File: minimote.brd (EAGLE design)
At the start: 85.6 x 54.2 mm, 44 parts, among them IC1 ATTINY841, J1 AVR_SPI_PROG_3X2PTH, J2 EDGEUSB, P1 TOUCHPAD, P2 TOUCHPAD, P3 TOUCHPAD, P4 TOUCHPAD, P5 TOUCHPAD, P6 TOUCHPAD, P7 TOUCHPAD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

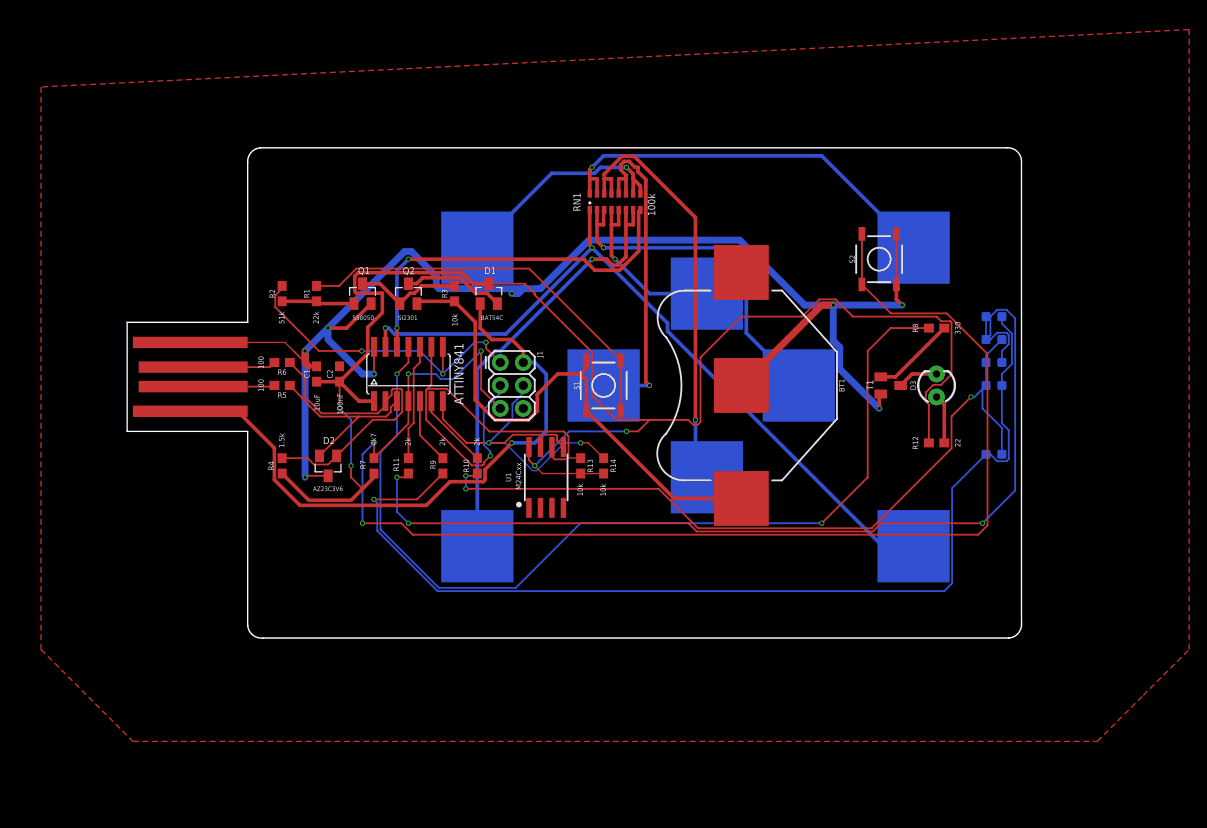
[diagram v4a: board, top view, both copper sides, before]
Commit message: Some board revisions and first firmware checkin
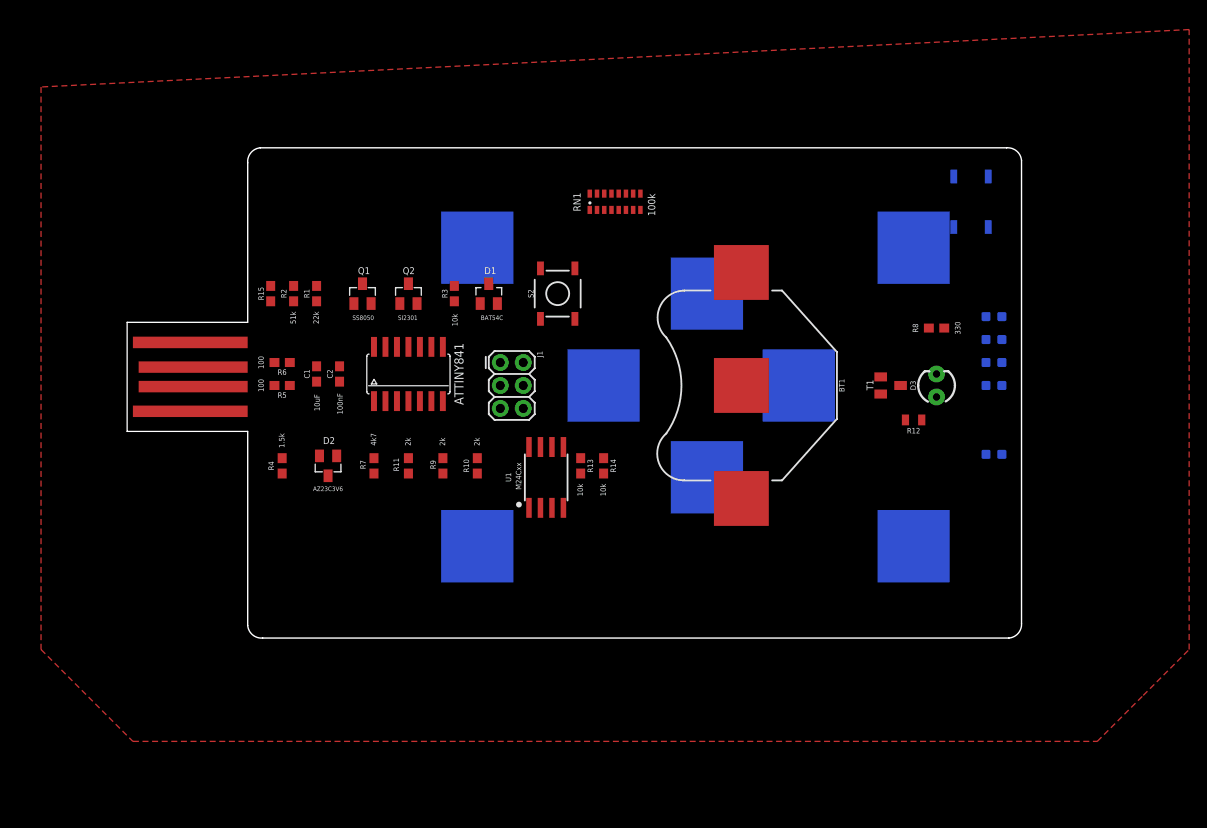
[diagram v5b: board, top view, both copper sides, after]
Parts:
- added R15: 100k, SparkFun-Resistors:0603
- R12: device SparkFun-Resistors:0603 -> SparkFun-Resistors:0805
- moved S1 45.4 mm to (80.0, 48.3), flipped to the bottom
- moved S2 35.8 mm to (34.3, 38.1)
- moved R12 3.59 mm to (73.7, 24.1), turned to 180 degrees
- moved R2 1.27 mm to (5.08, 38.1)
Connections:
- removed net N$5: D1.2, Q2.3
- new net LEDVCC: D1.2, Q2.3, R12.2
- net D_M: no longer D2.2
- net D_P: no longer D2.1, R4.1
- net GND: now also R15.1
- net MISO: now also R15.2
- net N$1: now also R12.1; no longer R12.2
- net N$8: now also D2.1, J2.DP, R6.2; no longer J2.DM, R5.2
- net N$9: now also D2.2, J2.DM, R4.1, R5.2; no longer J2.DP, R6.2
- net VCC: no longer R12.1
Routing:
- net VCC: track 176.8 -> 0.00 mm, vias 4 -> 0
- net GND: track 167.5 -> 0.00 mm, vias 8 -> 0
- net RST: track 150.4 -> 0.00 mm, vias 4 -> 0
- net N$125: track 114.9 -> 0.00 mm, vias 1 -> 0
- net N$123: track 110.5 -> 0.00 mm, vias 3 -> 0
- net LED4: track 104.9 -> 0.00 mm, vias 2 -> 0
- net N$124: track 85.3 -> 0.00 mm, vias 3 -> 0
- net PAD0: track 83.2 -> 0.00 mm, vias 2 -> 0
- net V_USB: track 69.0 -> 0.00 mm, vias 1 -> 0
- net VBAT: track 59.2 -> 0.00 mm
- net SCK: track 51.5 -> 0.00 mm, vias 1 -> 0
- net PAD6: track 49.4 -> 0.00 mm, vias 1 -> 0
- net PAD3: track 47.6 -> 0.00 mm, vias 1 -> 0
- net PAD1: track 45.8 -> 0.00 mm, vias 1 -> 0
- net N$7: track 44.2 -> 0.00 mm
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
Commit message: major pcb revisions
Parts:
- removed BT1: (no value), SparkFun-Batteries:BATTCON_20MM
- removed P1, P2, P3, P4, P5, P6, P7, P8: TOUCHPAD, minimote:TPAD
- added R16: 22M, SparkFun-Resistors:0603
- added U$1: BAT_AND_USB, minimote:PUNCHOUT_USB
- added U$2, U$3, U$4, U$5, U$6, U$7, U$8, U$9: BUTTON_RESISTIVE, minimote:BUTTON-CONDUCTIVE
- RN1: value 100k -> 10k
- moved R12 58.8 mm to (15.2, 30.5)
- moved R8 55.4 mm to (24.1, 53.3)
- moved T1 46.2 mm to (31.8, 52.1)
- moved S1 43.2 mm to (81.3, 5.08)
- moved R4 33.0 mm to (12.7, 50.8), turned to 90 degrees
- moved D2 32.5 mm to (8.38, 51.6), turned to 90 degrees
- moved U1 32.4 mm to (19.1, 47.0), turned to 270 degrees
- moved RN1 32.3 mm to (17.8, 25.4)
- moved R10 24.3 mm to (8.89, 36.8)
- moved J2 20.9 mm to (5.08, 43.2)
- moved R2 20.4 mm to (25.4, 36.8)
- moved R1 19.4 mm to (26.7, 41.9)
- moved R13 19.1 mm to (25.4, 3.81)
- moved R14 19.0 mm to (27.9, 3.81)
- moved R15 18.8 mm to (19.1, 29.2)
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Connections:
- removed net PAD0: IC1.13, P1.P$1, RN1.1
- removed net TOUCH2: IC1.12, RN1.8
- new net PA1: IC1.12
- new net PAD_HIGH: IC1.13, R16.1, U$2.2, U$3.2, U$4.2, U$5.2, U$6.2, U$7.2, U$8.2, U$9.2
- net GND: now also RN1.8, U$1.B-, U$2.1; no longer BT1.2
- net PAD1: now also U$3.1; no longer P2.P$1
- net PAD2: now also U$4.1; no longer P3.P$1
- net PAD3: now also U$5.1; no longer P4.P$1
- net PAD4: now also U$6.1; no longer P5.P$1
- net PAD5: now also U$7.1; no longer P6.P$1
- net PAD6: now also U$8.1; no longer P7.P$1
- net PAD7: now also U$9.1; no longer P8.P$1
- net VBAT: now also U$1.B+; no longer BT1.1
- net VCC: now also R16.2, RN1.1
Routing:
- added copper zone on layer 16, net GND
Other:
- outline, holes or cut-outs redrawn

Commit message: added library
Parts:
- moved D3 15.2 mm to (82.5, 25.4)
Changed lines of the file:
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@@
 <attribute name="VALUE" x="28.575" y="53.975" size="1.27" layer="27" rot="R270"/>
 </element>
-<element name="D3" library="minimote" package="LED_3MM" value="" x="82.55" y="40.64" rot="R90">
-<attribute name="PROD_ID" value="DIO-08794" x="82.55" y="40.64" size="1.778" layer="27" rot="R90" display="off"/>
+<element name="D3" library="minimote" package="LED_3MM" value="" x="82.55" y="25.4" rot="R90">
+<attribute name="PROD_ID" value="DIO-08794" x="82.55" y="25.4" size="1.778" layer="27" rot="R90" display="off"/>
 </element>
 <element name="U1" library="SparkFun-IC-Memory" library_urn="urn:adsk.eagle:library:524" package="SO08-EIAJ" package3d_urn="urn:adsk.eagle:package:38842/1" value="M24Cxx" x="19.05" y="46.99" smashed="yes" rot="R270">
@@
 <contactref element="T1" pad="C"/>
 <contactref element="D3" pad="K"/>
-<wire x1="32.85" y1="52.07" x2="82.55" y2="41.91" width="0" layer="19" extent="1-1"/>
+<wire x1="32.85" y1="52.07" x2="82.55" y2="26.67" width="0" layer="19" extent="1-1"/>
 </signal>
 <signal name="V_USB">
@@
 <contactref element="D3" pad="A"/>
 <contactref element="R12" pad="1"/>
-<wire x1="16.14" y1="30.48" x2="82.55" y2="39.37" width="0" layer="19" extent="1-1"/>
+<wire x1="16.14" y1="30.48" x2="82.55" y2="24.13" width="0" layer="19" extent="1-1"/>
 </signal>
 </signals>

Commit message: pause commit
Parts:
- added PAD1: (no value), wirepad:2,15/1,0
- moved R14 42.7 mm to (24.8, 46.4), turned to 90 degrees
- moved R13 42.6 mm to (26.4, 46.4), turned to 90 degrees
- moved U$7 37.1 mm to (71.6, 47.2)
- moved U$6 35.9 mm to (54.9, 15.2)
- moved U$3 34.3 mm to (38.1, 47.2)
- moved R1 32.2 mm to (1.14, 22.4), turned to 90 degrees
- moved T1 31.3 mm to (21.0, 22.7)
- moved R8 29.4 mm to (17.8, 24.6), turned to 270 degrees
- moved R2 26.8 mm to (2.79, 22.4), turned to 90 degrees
- moved R3 20.2 mm to (6.99, 29.8), turned to 270 degrees
- moved U$2 19.3 mm to (42.7, 29.0)
- moved J1 17.9 mm to (12.2, 31.4)
- moved U$4 17.5 mm to (38.1, 10.7)
- moved RN1 17.0 mm to (28.4, 38.6), turned to 270 degrees
- moved U$8 16.8 mm to (71.6, 10.7)
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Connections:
- net PA1: now also PAD1.1
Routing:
- net N$124: track 0.00 -> 226.3 mm, vias 0 -> 1
- net N$125: track 0.00 -> 135.7 mm, vias 0 -> 1
- net N$123: track 0.00 -> 126.5 mm, vias 0 -> 3
- net N$7: track 0.00 -> 106.0 mm, vias 0 -> 1
- net VBAT: track 0.00 -> 105.5 mm, vias 0 -> 1
- net N$2: track 0.00 -> 103.2 mm
- net N$1: track 0.00 -> 101.9 mm
- net RST: track 0.00 -> 65.9 mm
- net SCK: track 0.00 -> 47.6 mm
- net VCC: track 0.00 -> 47.1 mm
- net MOSI: track 0.00 -> 39.0 mm
- net MISO: track 0.00 -> 32.2 mm, vias 0 -> 1
- net LEDVCC: track 0.00 -> 25.8 mm
- net V_USB: track 0.00 -> 22.0 mm, vias 0 -> 1
- net LED4: track 0.00 -> 20.0 mm
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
